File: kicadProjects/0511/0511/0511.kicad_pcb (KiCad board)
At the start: 2 copper layers, 102 parts, among them SW1 SW_Push, SW10 SW_Push, SW11 SW_Push, SW12 SW_Push, SW13 SW_Push, SW14 SW_Push, SW15 SW_Push, SW16 SW_Push, SW17 SW_Push, SW18 SW_Push, SW19 SW_Push, SW2 SW_Push, SW20 SW_Push, SW21 SW_Push, SW22 SW_Push, SW23 SW_Push, SW24 SW_Push, SW25 SW_Push, SW26 SW_Push, SW27 SW_Push, SW28 SW_Push, SW29 SW_Push, SW3 SW_Push, SW30 SW_Push, SW31 SW_Push, SW32 SW_Push, SW33 SW_Push, SW34 SW_Push, SW35 SW_Push, SW36 SW_Push, SW37 SW_Push, SW38 SW_Push, SW39 SW_Push, SW4 SW_Push, SW40 SW_Push, SW41 SW_Push, SW42 SW_Push, SW43 SW_Push, SW44 SW_Push, SW45 SW_Push, SW46 SW_Push, SW47 SW_Push, SW48 SW_Push, SW5 SW_Push, SW6 SW_Push, SW7 SW_Push, SW8 SW_Push, SW9 SW_Push, U1 MCP23017, U2 YAAJ_BlackPill, U3 MCP23017, U4 MCP23017

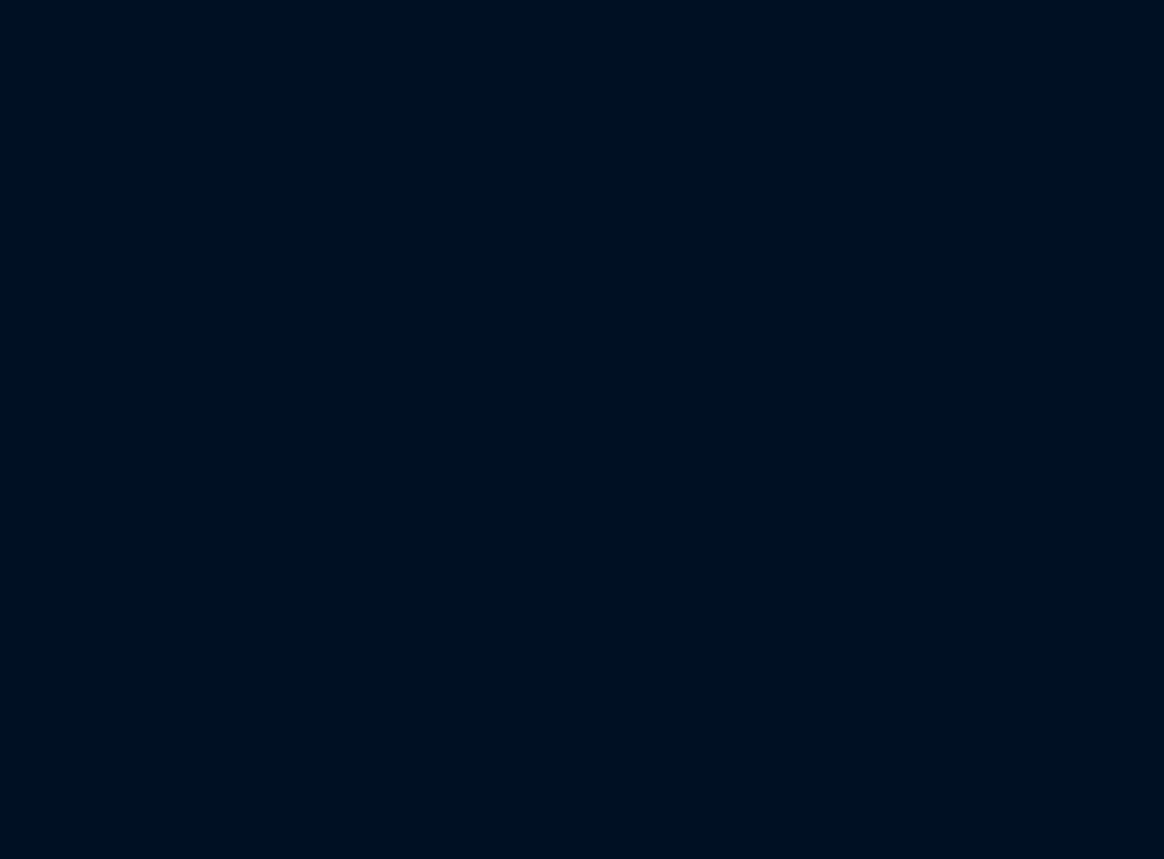
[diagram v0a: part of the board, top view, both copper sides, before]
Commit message: poursuite schema
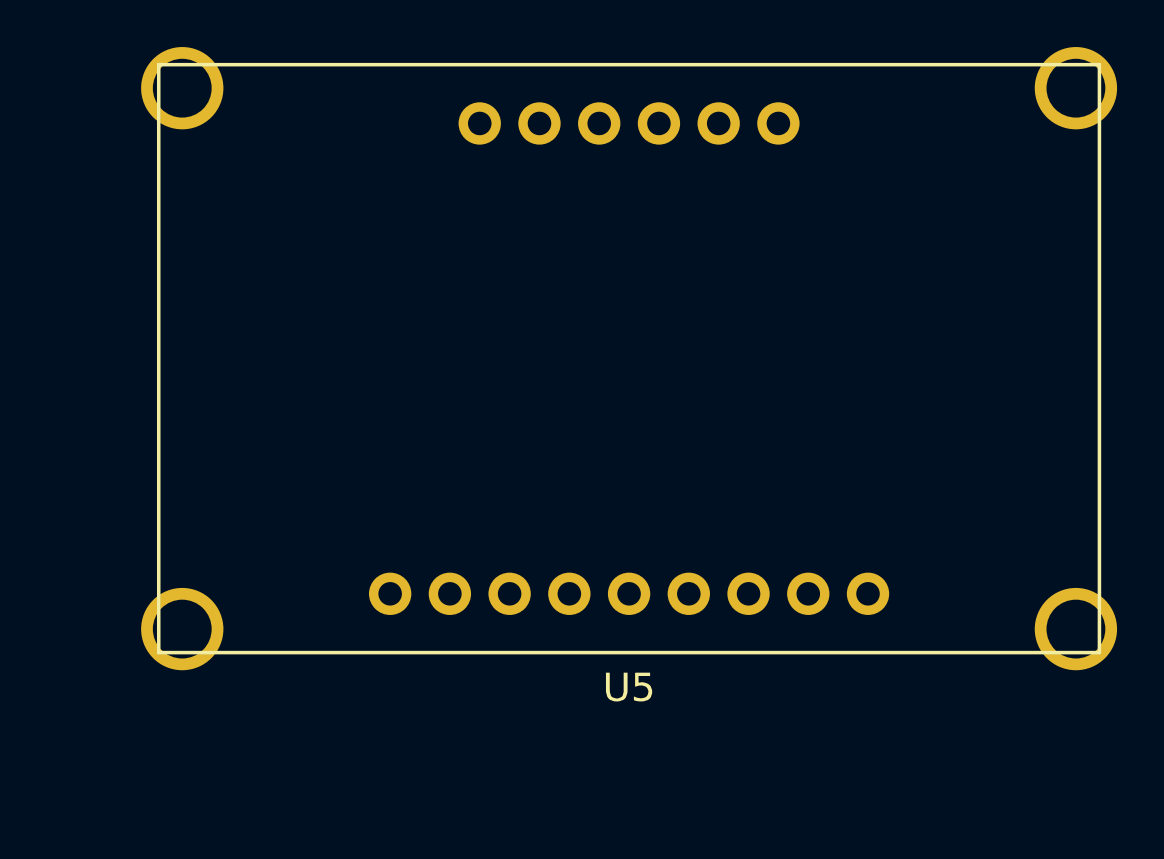
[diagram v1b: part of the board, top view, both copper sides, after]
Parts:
- added U5: UDA1334A_Breakout, Adafruit_UDA1334A:PinHeader_1x07_2.54mm, F.Cu at (244.0, 32.0)
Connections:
- U2 pad 27: unconnected-(U2-PA4-Pad27) -> Net-(U2-PA4)
- U2 pad 28: unconnected-(U2-PA5-Pad28) -> Net-(U2-PA5)
- U2 pad 30: unconnected-(U2-PA7-Pad30) -> Net-(U2-PA7)

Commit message: poursuite
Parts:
- moved U4 245.7 mm to (271.9, -77.1)
- moved R34 151.6 mm to (244.5, 90.5)
- moved SW29 115.0 mm to (240.5, 49.4)
- moved U5 108.0 mm to (302.1, 123.0)
- moved U2 94.7 mm to (238.0, 120.9)
- moved SW41 75.1 mm to (225.3, 49.6)
- moved SW35 75.1 mm to (210.2, 49.6)
- moved SW15 74.0 mm to (172.4, 35.0)
- moved SW21 74.0 mm to (187.5, 35.0)
- moved SW27 74.0 mm to (202.6, 35.0)
- moved SW3 74.0 mm to (142.2, 35.0)
- moved SW39 74.0 mm to (232.8, 35.0)
- moved SW9 74.0 mm to (157.3, 35.0)
- moved SW33 74.0 mm to (217.7, 35.0)
- moved SW12 70.3 mm to (143.2, 64.0)
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
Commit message: rectifications, modif empreinte capteur fsr, correctifs warnings
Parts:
- R1: value 4.7k -> R_Variable; footprint Resistor_THT:R_Axial_DIN0207_L6.3mm_D2.5mm_P7.62mm_Horizontal -> Connector_PinHeader_2.54mm:PinHeader_1x02_P2.54mm_Vertical
- R17, R33: value ~ -> R
- R19: value R -> ~
- R2: value 4.7k -> ~
- R3, R4: value R -> 4.7k
- R34: value R_Variable -> R; footprint Button_Switch_THT:Push_E-Switch_KS01Q01 -> Resistor_THT:R_Axial_DIN0207_L6.3mm_D2.5mm_P7.62mm_Horizontal
- U1: value MCP23017 -> UDA1334A_Breakout; footprint Package_DIP:DIP-28_W7.62mm -> Adafruit_UDA1334A:PinHeader_1x07_2.54mm
- U5: value UDA1334A_Breakout -> MCP23017; footprint Adafruit_UDA1334A:PinHeader_1x07_2.54mm -> Package_DIP:DIP-28_W7.62mm
- moved U4 221.4 mm to (163.5, 116.0)
- moved R34 164.1 mm to (88.1, 140.3)
- moved U5 128.1 mm to (174.3, 116.0)
- moved SW29 111.3 mm to (135.5, 86.2)
- moved U2 100.9 mm to (189.7, 32.4)
- moved R1 95.4 mm to (155.5, 155.5)
- moved SW15 70.4 mm to (105.3, 56.0)
- moved SW21 70.4 mm to (120.4, 56.0)
- moved SW27 70.4 mm to (135.5, 56.0)
- moved SW3 70.4 mm to (75.1, 56.0)
- moved SW39 70.4 mm to (165.6, 56.0)
- moved SW9 70.4 mm to (90.2, 56.0)
- moved SW33 70.4 mm to (150.6, 56.0)
- moved SW41 70.0 mm to (165.6, 86.2)
- moved SW35 70.0 mm to (150.6, 86.2)
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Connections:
- R1 pad 1: Net-(R1-Pad1) -> Net-(U1-3V)
- R1 pad 2: Net-(U1-A0) -> Net-(U2-PA1)
- R10 pad 2: Net-(U1-A0) -> Net-(U3-A0)
- R11 pad 2: Net-(U1-A0) -> Net-(U3-A0)
- R12 pad 2: Net-(U1-A0) -> Net-(U3-A0)
- R13 pad 2: Net-(U1-A0) -> Net-(U3-A0)
- R14 pad 2: Net-(U1-A0) -> Net-(U3-A0)
- R15 pad 2: Net-(U1-A0) -> Net-(U3-A0)
- R16 pad 2: Net-(U1-A0) -> Net-(U3-A0)
- R17 pad 2: Net-(R17-Pad2) -> Net-(U3-A0)
- R18 pad 2: Net-(R17-Pad2) -> Net-(U3-A0)
- R19 pad 2: Net-(R17-Pad2) -> Net-(R19-Pad2)
- R2 pad 1: Net-(R2-Pad1) -> Net-(U2-PA1)
- R2 pad 2: Net-(U1-A0) -> Net-(U3-A0)
- R20 pad 2: Net-(R17-Pad2) -> Net-(R19-Pad2)
- R21 pad 2: Net-(R17-Pad2) -> Net-(R19-Pad2)
- R22 pad 2: Net-(R17-Pad2) -> Net-(R19-Pad2)
- R23 pad 2: Net-(R17-Pad2) -> Net-(R19-Pad2)
- R24 pad 2: Net-(R17-Pad2) -> Net-(R19-Pad2)
- R25 pad 2: Net-(R17-Pad2) -> Net-(R19-Pad2)
- R26 pad 2: Net-(U1-A0) -> Net-(R19-Pad2)
- R27 pad 2: Net-(U1-A0) -> Net-(R19-Pad2)
- R28 pad 2: Net-(U1-A0) -> Net-(U3-A0)
- R29 pad 2: Net-(U1-A0) -> Net-(U3-A0)
- R3 pad 2: Net-(U1-A0) -> Net-(U3-A0)
- R30 pad 2: Net-(U1-A0) -> Net-(U3-A0)
- R31 pad 2: Net-(U1-A0) -> Net-(U3-A0)
- R32 pad 2: Net-(U1-A0) -> Net-(U3-A0)
- R33 pad 2: Net-(U1-A0) -> Net-(U3-A0)
- R34 pad 1: Net-(U1-SCL) -> Net-(R34-Pad1)
- R34 pad 2: Net-(U2-PA1) -> Net-(U3-A0)
- R35 pad 1: Net-(U2-PA1) -> Net-(R35-Pad1)
- R35 pad 2: Net-(U1-A0) -> Net-(U3-A0)
- R36 pad 2: Net-(U1-A0) -> Net-(U3-A0)
- R37 pad 2: Net-(U1-A0) -> Net-(U3-A0)
- R38 pad 2: Net-(U1-A0) -> Net-(U3-A0)
- R39 pad 2: Net-(U1-A0) -> Net-(U3-A0)
- R4 pad 2: Net-(U1-A0) -> Net-(U3-A0)
- R40 pad 2: Net-(U1-A0) -> Net-(U3-A0)
- R41 pad 2: Net-(U1-A0) -> Net-(U3-A0)
- R42 pad 2: Net-(U1-A0) -> Net-(U3-A0)
- R43 pad 2: Net-(U1-A0) -> Net-(U3-A0)
- R44 pad 2: Net-(U1-A0) -> Net-(U3-A0)
- R45 pad 2: Net-(U1-A0) -> Net-(U3-A0)
- R46 pad 2: Net-(U1-A0) -> Net-(U3-A0)
- R47 pad 2: Net-(U1-A0) -> Net-(U3-A0)
- R48 pad 2: Net-(U1-A0) -> Net-(U3-A0)
- R49 pad 2: Net-(U1-A0) -> Net-(U3-A0)
- R5 pad 2: Net-(U1-A0) -> Net-(U3-A0)
- R50 pad 2: Net-(U1-A0) -> Net-(U3-A0)
- R6 pad 2: Net-(U1-A0) -> Net-(U3-A0)
- R7 pad 2: Net-(U1-A0) -> Net-(U3-A0)
- R8 pad 2: Net-(U1-A0) -> Net-(U3-A0)
- R9 pad 2: Net-(U1-A0) -> Net-(U3-A0)
- SW1 pad 1: Net-(R1-Pad1) -> Net-(R3-Pad1)
- SW1 pad 2: Net-(U1-GPA7) -> Net-(U3-GPA7)
- SW10 pad 1: Net-(R10-Pad1) -> Net-(R12-Pad1)
- SW10 pad 2: Net-(U1-GPB6) -> Net-(U3-GPB6)
- SW11 pad 1: Net-(R11-Pad1) -> Net-(R13-Pad1)
- SW11 pad 2: Net-(U1-GPB5) -> Net-(U3-GPB5)
- SW12 pad 1: Net-(R12-Pad1) -> Net-(R14-Pad1)
- SW12 pad 2: Net-(U1-GPB4) -> Net-(U3-GPB4)
- SW13 pad 1: Net-(R13-Pad1) -> Net-(R15-Pad1)
- SW13 pad 2: Net-(U1-GPB3) -> Net-(U3-GPB3)
- SW14 pad 1: Net-(R14-Pad1) -> Net-(R16-Pad1)
- SW14 pad 2: Net-(U1-GPB2) -> Net-(U3-GPB2)
- SW15 pad 1: Net-(R15-Pad1) -> Net-(R17-Pad1)
- SW15 pad 2: Net-(U1-GPB1) -> Net-(U3-GPB1)
- SW16 pad 1: Net-(R16-Pad1) -> Net-(R18-Pad1)
- SW16 pad 2: Net-(U1-GPB0) -> Net-(U3-GPB0)
- SW17 pad 1: Net-(R17-Pad1) -> Net-(R19-Pad1)
- SW17 pad 2: Net-(U3-GPA7) -> Net-(U4-GPA7)
- SW18 pad 1: Net-(R18-Pad1) -> Net-(R20-Pad1)
- SW18 pad 2: Net-(U3-GPA6) -> Net-(U4-GPA6)
- SW19 pad 1: Net-(R19-Pad1) -> Net-(R21-Pad1)
- SW19 pad 2: Net-(U3-GPA5) -> Net-(U4-GPA5)
- SW2 pad 1: Net-(R2-Pad1) -> Net-(R4-Pad1)
- SW2 pad 2: Net-(U1-GPA6) -> Net-(U3-GPA6)
- SW20 pad 1: Net-(R20-Pad1) -> Net-(R22-Pad1)
- SW20 pad 2: Net-(U3-GPA4) -> Net-(U4-GPA4)
- SW21 pad 1: Net-(R21-Pad1) -> Net-(R23-Pad1)
- SW21 pad 2: Net-(U3-GPA3) -> Net-(U4-GPA3)
- SW22 pad 1: Net-(R22-Pad1) -> Net-(R24-Pad1)
- SW22 pad 2: Net-(U3-GPA2) -> Net-(U4-GPA2)
- SW23 pad 1: Net-(R23-Pad1) -> Net-(R25-Pad1)
- SW23 pad 2: Net-(U3-GPA1) -> Net-(U4-GPA1)
- SW24 pad 1: Net-(R24-Pad1) -> Net-(R26-Pad1)
- SW24 pad 2: Net-(U3-GPA0) -> Net-(U4-GPA0)
- SW25 pad 1: Net-(R25-Pad1) -> Net-(R27-Pad1)
- SW25 pad 2: Net-(U3-GPB7) -> Net-(U4-GPB7)
- SW26 pad 1: Net-(R26-Pad1) -> Net-(R28-Pad1)
- SW26 pad 2: Net-(U3-GPB6) -> Net-(U4-GPB6)
- SW27 pad 1: Net-(R27-Pad1) -> Net-(R29-Pad1)
- SW27 pad 2: Net-(U3-GPB5) -> Net-(U4-GPB5)
- SW28 pad 1: Net-(R28-Pad1) -> Net-(R30-Pad1)
- SW28 pad 2: Net-(U3-GPB4) -> Net-(U4-GPB4)
- SW29 pad 1: Net-(R29-Pad1) -> Net-(R31-Pad1)
- SW29 pad 2: Net-(U3-GPB3) -> Net-(U4-GPB3)
- SW3 pad 1: Net-(R3-Pad1) -> Net-(R5-Pad1)
- SW3 pad 2: Net-(U1-GPA5) -> Net-(U3-GPA5)
- SW30 pad 1: Net-(R30-Pad1) -> Net-(R32-Pad1)
- SW30 pad 2: Net-(U3-GPB2) -> Net-(U4-GPB2)
- SW31 pad 1: Net-(R31-Pad1) -> Net-(R33-Pad1)
- SW31 pad 2: Net-(U3-GPB1) -> Net-(U4-GPB1)
- SW32 pad 1: Net-(R32-Pad1) -> Net-(R34-Pad1)
- SW32 pad 2: Net-(U3-GPB0) -> Net-(U4-GPB0)
- SW33 pad 1: Net-(R33-Pad1) -> Net-(R35-Pad1)
- SW33 pad 2: Net-(U4-GPA7) -> Net-(U5-GPA7)
- SW34 pad 2: Net-(U4-GPA6) -> Net-(U5-GPA6)
- SW35 pad 2: Net-(U4-GPA5) -> Net-(U5-GPA5)
- SW36 pad 2: Net-(U4-GPA4) -> Net-(U5-GPA4)
- SW37 pad 2: Net-(U4-GPA3) -> Net-(U5-GPA3)
- SW38 pad 2: Net-(U4-GPA2) -> Net-(U5-GPA2)
- SW39 pad 2: Net-(U4-GPA1) -> Net-(U5-GPA1)
- SW4 pad 1: Net-(R4-Pad1) -> Net-(R6-Pad1)
- SW4 pad 2: Net-(U1-GPA4) -> Net-(U3-GPA4)
- SW40 pad 2: Net-(U4-GPA0) -> Net-(U5-GPA0)
- SW41 pad 2: Net-(U4-GPB7) -> Net-(U5-GPB7)
- SW42 pad 2: Net-(U4-GPB6) -> Net-(U5-GPB6)
- SW43 pad 2: Net-(U4-GPB5) -> Net-(U5-GPB5)
- SW44 pad 2: Net-(U4-GPB4) -> Net-(U5-GPB4)
- SW45 pad 2: Net-(U4-GPB3) -> Net-(U5-GPB3)
- SW46 pad 2: Net-(U4-GPB2) -> Net-(U5-GPB2)
- SW47 pad 2: Net-(U4-GPB1) -> Net-(U5-GPB1)
- SW48 pad 2: Net-(U4-GPB0) -> Net-(U5-GPB0)
- SW5 pad 1: Net-(R5-Pad1) -> Net-(R7-Pad1)
- SW5 pad 2: Net-(U1-GPA3) -> Net-(U3-GPA3)
- SW6 pad 1: Net-(R6-Pad1) -> Net-(R8-Pad1)
- SW6 pad 2: Net-(U1-GPA2) -> Net-(U3-GPA2)
- SW7 pad 1: Net-(R7-Pad1) -> Net-(R9-Pad1)
- SW7 pad 2: Net-(U1-GPA1) -> Net-(U3-GPA1)
- SW8 pad 1: Net-(R8-Pad1) -> Net-(R10-Pad1)
- SW8 pad 2: Net-(U1-GPA0) -> Net-(U3-GPA0)
- SW9 pad 1: Net-(R9-Pad1) -> Net-(R11-Pad1)
- SW9 pad 2: Net-(U1-GPB7) -> Net-(U3-GPB7)
- U1 pad 1: Net-(U1-GPB0) -> unconnected-(U1-VIN-Pad1)
- U1 pad 10: unconnected-(U1-VSS-Pad10) -> (no net)
- U1 pad 11: unconnected-(U1-NC-Pad11) -> (no net)
- U1 pad 12: Net-(U1-SCL) -> (no net)
- U1 pad 13: Net-(U1-SCL) -> (no net)
- U1 pad 14: unconnected-(U1-NC-Pad14) -> (no net)
- U1 pad 15: Net-(U1-A0) -> (no net)
- U1 pad 2: Net-(U1-GPB1) -> Net-(U1-3V)
- U1 pad 3: Net-(U1-GPB2) -> unconnected-(U1-GND-Pad3)
- U1 pad 4: Net-(U1-GPB3) -> Net-(U1-WSEL)
- U1 pad 5: Net-(U1-GPB4) -> Net-(U1-BCLK)
- U1 pad 6: Net-(U1-GPB5) -> Net-(U1-DIN)
- U1 pad 7: Net-(U1-GPB6) -> (no net)
- U1 pad 8: Net-(U1-GPB7) -> (no net)
- U1 pad 9: unconnected-(U1-VDD-Pad9) -> (no net)
- U2 pad 16: Net-(U1-SCL) -> Net-(U1-3V)
- U2 pad 17: Net-(U1-A0) -> Net-(U3-A0)
- U2 pad 18: Net-(U1-A0) -> Net-(U3-A0)
- U2 pad 19: Net-(U1-SCL) -> Net-(U1-3V)
- U2 pad 20: Net-(U1-SCL) -> Net-(U1-3V)
- U2 pad 27: Net-(U2-PA4) -> Net-(U1-WSEL)
- U2 pad 28: Net-(U2-PA5) -> Net-(U1-BCLK)
- U2 pad 30: Net-(U2-PA7) -> Net-(U1-DIN)
- U3 pad 12: Net-(U1-SCL) -> Net-(U1-3V)
- U3 pad 13: Net-(U1-SCL) -> Net-(U1-3V)
- U3 pad 15: Net-(U1-A0) -> Net-(U3-A0)
- U3 pad 16: Net-(U1-SCL) -> Net-(U3-A0)
- U3 pad 17: Net-(U1-SCL) -> Net-(U3-A0)
- U4 pad 12: Net-(U1-SCL) -> Net-(U1-3V)
- U4 pad 13: Net-(U1-SCL) -> Net-(U1-3V)
- U4 pad 15: Net-(U1-SCL) -> Net-(U3-A0)
- U4 pad 16: Net-(U1-SCL) -> Net-(U1-3V)
- U4 pad 17: Net-(U1-SCL) -> Net-(U1-3V)
- U4 pad 18: Net-(U1-SCL) -> unconnected-(U4-~{RESET}-Pad18)
- U4 pad 19: Net-(U1-SCL) -> unconnected-(U4-INTB-Pad19)
- U4 pad 20: Net-(U1-SCL) -> unconnected-(U4-INTA-Pad20)
- U5 pad 1: unconnected-(U5-VIN-Pad1) -> Net-(U5-GPB0)
- U5 pad 10: (no net) -> unconnected-(U5-VSS-Pad10)
- U5 pad 11: (no net) -> unconnected-(U5-NC-Pad11)
- U5 pad 12: (no net) -> Net-(U1-3V)
- U5 pad 13: (no net) -> Net-(U1-3V)
- U5 pad 14: (no net) -> unconnected-(U5-NC-Pad14)
- U5 pad 15: (no net) -> Net-(U1-3V)
- U5 pad 2: Net-(U1-SCL) -> Net-(U5-GPB1)
- U5 pad 3: unconnected-(U5-GND-Pad3) -> Net-(U5-GPB2)
- U5 pad 4: Net-(U2-PA4) -> Net-(U5-GPB3)
- U5 pad 5: Net-(U2-PA5) -> Net-(U5-GPB4)
- U5 pad 6: Net-(U2-PA7) -> Net-(U5-GPB5)
- U5 pad 7: (no net) -> Net-(U5-GPB6)
- U5 pad 8: (no net) -> Net-(U5-GPB7)
- U5 pad 9: (no net) -> unconnected-(U5-VDD-Pad9)

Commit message: ajout empreintes
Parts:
- removed R41, R42, R43, R44, R45, R46, R47, R48, R49, R50: R, Resistor_THT:R_Axial_DIN0207_L6.3mm_D2.5mm_P7.62mm_Horizontal
- removed SW33, SW34, SW35, SW36, SW37, SW38, SW39, SW40, SW41, SW42, SW43, SW44, SW45, SW46, SW47, SW48: SW_Push, Button_Switch_Keyboard:SW_Cherry_MX_1.00u_PCB
- removed U5: MCP23017, Package_DIP:DIP-28_W7.62mm
- added C1: C, Capacitor_THT:C_Disc_D3.0mm_W1.6mm_P2.50mm, F.Cu at (287.0, 157.0)
- added C10: C, Capacitor_THT:C_Disc_D3.0mm_W1.6mm_P2.50mm, F.Cu at (271.1, 142.4)
- added C11: C, Capacitor_THT:C_Disc_D3.0mm_W1.6mm_P2.50mm, F.Cu at (255.2, 133.1)
- added C12: C, Capacitor_THT:C_Disc_D3.0mm_W1.6mm_P2.50mm, F.Cu at (239.3, 133.1)
- added C13: C, Capacitor_THT:C_Disc_D3.0mm_W1.6mm_P2.50mm, F.Cu at (223.4, 95.5)
- added C14: C, Capacitor_THT:C_Disc_D3.0mm_W1.6mm_P2.50mm, F.Cu at (271.1, 133.1)
- added C15: C, Capacitor_THT:C_Disc_D3.0mm_W1.6mm_P2.50mm, F.Cu at (223.4, 133.1)
- added C16: C, Capacitor_THT:C_Disc_D3.0mm_W1.6mm_P2.50mm, F.Cu at (223.4, 161.2)
- added C17: C, Capacitor_THT:C_Disc_D3.0mm_W1.6mm_P2.50mm, F.Cu at (271.1, 151.8)
- added C18: C, Capacitor_THT:C_Disc_D3.0mm_W1.6mm_P2.50mm, F.Cu at (223.4, 114.2)
- added C19: C, Capacitor_THT:C_Disc_D3.0mm_W1.6mm_P2.50mm, F.Cu at (255.2, 123.7)
- added C2: C, Capacitor_THT:C_Disc_D3.0mm_W1.6mm_P2.50mm, F.Cu at (255.2, 161.2)
- added C20: C, Capacitor_THT:C_Disc_D3.0mm_W1.6mm_P2.50mm, F.Cu at (271.1, 114.2)
- added C21: C, Capacitor_THT:C_Disc_D3.0mm_W1.6mm_P2.50mm, F.Cu at (271.1, 104.8)
- added C22: C, Capacitor_THT:C_Disc_D3.0mm_W1.6mm_P2.50mm, F.Cu at (271.1, 161.2)
- added C23: C, Capacitor_THT:C_Disc_D3.0mm_W1.6mm_P2.50mm, F.Cu at (223.4, 142.4)
- added C24: C, Capacitor_THT:C_Disc_D3.0mm_W1.6mm_P2.50mm, F.Cu at (239.3, 123.7)
- added C25: C, Capacitor_THT:C_Disc_D3.0mm_W1.6mm_P2.50mm, F.Cu at (239.3, 151.8)
- added C26: C, Capacitor_THT:C_Disc_D3.0mm_W1.6mm_P2.50mm, F.Cu at (239.3, 142.4)
- added C27: C, Capacitor_THT:C_Disc_D3.0mm_W1.6mm_P2.50mm, F.Cu at (255.2, 95.5)
- added C28: C, Capacitor_THT:C_Disc_D3.0mm_W1.6mm_P2.50mm, F.Cu at (223.4, 104.8)
- added C29: C, Capacitor_THT:C_Disc_D3.0mm_W1.6mm_P2.50mm, F.Cu at (239.3, 104.8)
- added C3: C, Capacitor_THT:C_Disc_D3.0mm_W1.6mm_P2.50mm, F.Cu at (223.4, 123.7)
- added C30: C, Capacitor_THT:C_Disc_D3.0mm_W1.6mm_P2.50mm, F.Cu at (223.4, 151.8)
- added C31: C, Capacitor_THT:C_Disc_D3.0mm_W1.6mm_P2.50mm, F.Cu at (239.3, 95.5)
- added C32: C, Capacitor_THT:C_Disc_D3.0mm_W1.6mm_P2.50mm, F.Cu at (271.1, 123.7)
- added C33: C, Capacitor_THT:C_Disc_D3.0mm_W1.6mm_P2.50mm, F.Cu at (239.3, 161.2)
- added C4: C, Capacitor_THT:C_Disc_D3.0mm_W1.6mm_P2.50mm, F.Cu at (239.3, 114.2)
- added C5: C, Capacitor_THT:C_Disc_D3.0mm_W1.6mm_P2.50mm, F.Cu at (255.2, 104.8)
- added C6: C, Capacitor_THT:C_Disc_D3.0mm_W1.6mm_P2.50mm, F.Cu at (271.1, 95.5)
- added C7: C, Capacitor_THT:C_Disc_D3.0mm_W1.6mm_P2.50mm, F.Cu at (255.2, 114.2)
- added C8: C, Capacitor_THT:C_Disc_D3.0mm_W1.6mm_P2.50mm, F.Cu at (255.2, 142.4)
- added C9: C, Capacitor_THT:C_Disc_D3.0mm_W1.6mm_P2.50mm, F.Cu at (255.2, 151.8)
- added D1: LED, Diode_THT:D_DO-41_SOD81_P10.16mm_Horizontal, F.Cu at (255.5, 157.6)
- added D10: LED, Diode_THT:D_DO-41_SOD81_P10.16mm_Horizontal, F.Cu at (255.5, 129.3)
- added D11: LED, Diode_THT:D_DO-41_SOD81_P10.16mm_Horizontal, F.Cu at (239.6, 129.3)
- added D12: LED, Diode_THT:D_DO-41_SOD81_P10.16mm_Horizontal, F.Cu at (223.7, 91.8)
- added D13: LED, Diode_THT:D_DO-41_SOD81_P10.16mm_Horizontal, F.Cu at (271.4, 129.3)
- added D14: LED, Diode_THT:D_DO-41_SOD81_P10.16mm_Horizontal, F.Cu at (223.7, 129.3)
- added D15: LED, Diode_THT:D_DO-41_SOD81_P10.16mm_Horizontal, F.Cu at (223.7, 157.6)
- added D16: LED, Diode_THT:D_DO-41_SOD81_P10.16mm_Horizontal, F.Cu at (271.4, 148.2)
- added D17: LED, Diode_THT:D_DO-41_SOD81_P10.16mm_Horizontal, F.Cu at (223.7, 110.5)
- added D18: LED, Diode_THT:D_DO-41_SOD81_P10.16mm_Horizontal, F.Cu at (255.5, 120.0)
- added D19: LED, Diode_THT:D_DO-41_SOD81_P10.16mm_Horizontal, F.Cu at (271.4, 110.5)
- added D2: LED, Diode_THT:D_DO-41_SOD81_P10.16mm_Horizontal, F.Cu at (223.7, 120.0)
- added D20: LED, Diode_THT:D_DO-41_SOD81_P10.16mm_Horizontal, F.Cu at (271.4, 101.2)
- added D21: LED, Diode_THT:D_DO-41_SOD81_P10.16mm_Horizontal, F.Cu at (271.4, 157.6)
- added D22: LED, Diode_THT:D_DO-41_SOD81_P10.16mm_Horizontal, F.Cu at (223.7, 138.8)
- added D23: LED, Diode_THT:D_DO-41_SOD81_P10.16mm_Horizontal, F.Cu at (239.6, 120.0)
- added D24: LED, Diode_THT:D_DO-41_SOD81_P10.16mm_Horizontal, F.Cu at (239.6, 148.2)
- added D25: LED, Diode_THT:D_DO-41_SOD81_P10.16mm_Horizontal, F.Cu at (239.6, 138.8)
- added D26: LED, Diode_THT:D_DO-41_SOD81_P10.16mm_Horizontal, F.Cu at (255.5, 91.8)
- added D27: LED, Diode_THT:D_DO-41_SOD81_P10.16mm_Horizontal, F.Cu at (223.7, 101.2)
- added D28: LED, Diode_THT:D_DO-41_SOD81_P10.16mm_Horizontal, F.Cu at (239.6, 101.2)
- added D29: LED, Diode_THT:D_DO-41_SOD81_P10.16mm_Horizontal, F.Cu at (223.7, 148.2)
- added D3: LED, Diode_THT:D_DO-41_SOD81_P10.16mm_Horizontal, F.Cu at (239.6, 110.5)
- added D30: LED, Diode_THT:D_DO-41_SOD81_P10.16mm_Horizontal, F.Cu at (239.6, 91.8)
- added D31: LED, Diode_THT:D_DO-41_SOD81_P10.16mm_Horizontal, F.Cu at (271.4, 120.0)
- added D32: LED, Diode_THT:D_DO-41_SOD81_P10.16mm_Horizontal, F.Cu at (239.6, 157.6)
- added D4: LED, Diode_THT:D_DO-41_SOD81_P10.16mm_Horizontal, F.Cu at (255.5, 101.2)
- added D5: LED, Diode_THT:D_DO-41_SOD81_P10.16mm_Horizontal, F.Cu at (271.4, 91.8)
- added D6: LED, Diode_THT:D_DO-41_SOD81_P10.16mm_Horizontal, F.Cu at (255.5, 110.5)
- added D7: LED, Diode_THT:D_DO-41_SOD81_P10.16mm_Horizontal, F.Cu at (255.5, 138.8)
- added D8: LED, Diode_THT:D_DO-41_SOD81_P10.16mm_Horizontal, F.Cu at (255.5, 148.2)
- added D9: LED, Diode_THT:D_DO-41_SOD81_P10.16mm_Horizontal, F.Cu at (271.4, 138.8)
- R1: footprint Connector_PinHeader_2.54mm:PinHeader_1x02_P2.54mm_Vertical -> Button_Switch_THT:Push_E-Switch_KS01Q01
- R19, R35: value ~ -> R
- R3, R4: value 4.7k -> R
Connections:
- R10 pad 1: Net-(R10-Pad1) -> /Button_RCD1/To_MCP_PIN
- R10 pad 2: Net-(U3-A0) -> GND
- R11 pad 1: Net-(R11-Pad1) -> /Button_RCD2/To_MCP_PIN
- R11 pad 2: Net-(U3-A0) -> GND
- R12 pad 1: Net-(R12-Pad1) -> /Button_RCD3/To_MCP_PIN
- R12 pad 2: Net-(U3-A0) -> GND
- R13 pad 1: Net-(R13-Pad1) -> /Button_RCD4/To_MCP_PIN
- R13 pad 2: Net-(U3-A0) -> GND
- R14 pad 1: Net-(R14-Pad1) -> /Button_RCD5/To_MCP_PIN
- R14 pad 2: Net-(U3-A0) -> GND
- R15 pad 1: Net-(R15-Pad1) -> /Button_RCD6/To_MCP_PIN
- R15 pad 2: Net-(U3-A0) -> GND
- R16 pad 1: Net-(R16-Pad1) -> /Button_RCD7/To_MCP_PIN
- R16 pad 2: Net-(U3-A0) -> GND
- R17 pad 1: Net-(R17-Pad1) -> /Button_RCD8/To_MCP_PIN
- R17 pad 2: Net-(U3-A0) -> GND
- R18 pad 1: Net-(R18-Pad1) -> /Button_RCD9/To_MCP_PIN
- R18 pad 2: Net-(U3-A0) -> GND
- R19 pad 1: Net-(R19-Pad1) -> /Button_RCD10/To_MCP_PIN
- R19 pad 2: Net-(R19-Pad2) -> GND
- R2 pad 2: Net-(U3-A0) -> Net-(R2-Pad2)
- R20 pad 1: Net-(R20-Pad1) -> /Button_RCD11/To_MCP_PIN
- R20 pad 2: Net-(R19-Pad2) -> GND
- R21 pad 1: Net-(R21-Pad1) -> /Button_RCD12/To_MCP_PIN
- R21 pad 2: Net-(R19-Pad2) -> GND
- R22 pad 1: Net-(R22-Pad1) -> /Button_RCD13/To_MCP_PIN
- R22 pad 2: Net-(R19-Pad2) -> GND
- R23 pad 1: Net-(R23-Pad1) -> /Button_RCD14/To_MCP_PIN
- R23 pad 2: Net-(R19-Pad2) -> GND
- R24 pad 1: Net-(R24-Pad1) -> /Button_RCD15/To_MCP_PIN
- R24 pad 2: Net-(R19-Pad2) -> GND
- R25 pad 1: Net-(R25-Pad1) -> /Button_RCD16/To_MCP_PIN
- R25 pad 2: Net-(R19-Pad2) -> GND
- R26 pad 1: Net-(R26-Pad1) -> /Button_RCD17/To_MCP_PIN
- R26 pad 2: Net-(R19-Pad2) -> GND
- R27 pad 1: Net-(R27-Pad1) -> /Button_RCD18/To_MCP_PIN
- R27 pad 2: Net-(R19-Pad2) -> GND
- R28 pad 1: Net-(R28-Pad1) -> /Button_RCD19/To_MCP_PIN
- R28 pad 2: Net-(U3-A0) -> GND
- R29 pad 1: Net-(R29-Pad1) -> /Button_RCD20/To_MCP_PIN
- R29 pad 2: Net-(U3-A0) -> GND
- R3 pad 1: Net-(R3-Pad1) -> +3.3V
- R3 pad 2: Net-(U3-A0) -> Net-(U2-PB8)
- R30 pad 1: Net-(R30-Pad1) -> /Button_RCD21/To_MCP_PIN
- R30 pad 2: Net-(U3-A0) -> GND
- R31 pad 1: Net-(R31-Pad1) -> /Button_RCD22/To_MCP_PIN
- R31 pad 2: Net-(U3-A0) -> GND
- R32 pad 1: Net-(R32-Pad1) -> /Button_RCD23/To_MCP_PIN
- R32 pad 2: Net-(U3-A0) -> GND
- R33 pad 1: Net-(R33-Pad1) -> /Button_RCD24/To_MCP_PIN
- R33 pad 2: Net-(U3-A0) -> GND
- R34 pad 1: Net-(R34-Pad1) -> /Button_RCD25/To_MCP_PIN
- R34 pad 2: Net-(U3-A0) -> GND
- R35 pad 1: Net-(R35-Pad1) -> /Button_RCD26/To_MCP_PIN
- R35 pad 2: Net-(U3-A0) -> GND
- R36 pad 1: Net-(R36-Pad1) -> /Button_RCD27/To_MCP_PIN
- R36 pad 2: Net-(U3-A0) -> GND
- R37 pad 1: Net-(R37-Pad1) -> /Button_RCD28/To_MCP_PIN
- R37 pad 2: Net-(U3-A0) -> GND
- R38 pad 1: Net-(R38-Pad1) -> /Button_RCD29/To_MCP_PIN
- R38 pad 2: Net-(U3-A0) -> GND
- R39 pad 1: Net-(R39-Pad1) -> /Button_RCD30/To_MCP_PIN
- R39 pad 2: Net-(U3-A0) -> GND
- R4 pad 1: Net-(R4-Pad1) -> +3.3V
- R4 pad 2: Net-(U3-A0) -> Net-(U2-PB9)
- R40 pad 1: Net-(R40-Pad1) -> /Button_RCD31/To_MCP_PIN
- R40 pad 2: Net-(U3-A0) -> GND
- R5 pad 1: Net-(R5-Pad1) -> +3.3V
- R5 pad 2: Net-(U3-A0) -> Net-(U3-~{RESET})
- R6 pad 1: Net-(R6-Pad1) -> +3.3V
- R6 pad 2: Net-(U3-A0) -> Net-(U2-PB8)
- R7 pad 1: Net-(R7-Pad1) -> +3.3V
- R7 pad 2: Net-(U3-A0) -> Net-(U4-~{RESET})
- R8 pad 1: Net-(R8-Pad1) -> +3.3V
- R8 pad 2: Net-(U3-A0) -> Net-(U2-PB9)
- R9 pad 1: Net-(R9-Pad1) -> /Button_RCD/To_MCP_PIN
- R9 pad 2: Net-(U3-A0) -> GND
- SW1 pad 1: Net-(R3-Pad1) -> +3.3V
- SW1 pad 2: Net-(U3-GPA7) -> /Button_RCD/To_MCP_PIN
- SW10 pad 1: Net-(R12-Pad1) -> +3.3V
- SW10 pad 2: Net-(U3-GPB6) -> /Button_RCD9/To_MCP_PIN
- SW11 pad 1: Net-(R13-Pad1) -> +3.3V
- SW11 pad 2: Net-(U3-GPB5) -> /Button_RCD10/To_MCP_PIN
- SW12 pad 1: Net-(R14-Pad1) -> +3.3V
- SW12 pad 2: Net-(U3-GPB4) -> /Button_RCD11/To_MCP_PIN
- SW13 pad 1: Net-(R15-Pad1) -> +3.3V
- SW13 pad 2: Net-(U3-GPB3) -> /Button_RCD12/To_MCP_PIN
- SW14 pad 1: Net-(R16-Pad1) -> +3.3V
- SW14 pad 2: Net-(U3-GPB2) -> /Button_RCD13/To_MCP_PIN
- SW15 pad 1: Net-(R17-Pad1) -> +3.3V
- SW15 pad 2: Net-(U3-GPB1) -> /Button_RCD14/To_MCP_PIN
- SW16 pad 1: Net-(R18-Pad1) -> +3.3V
- SW16 pad 2: Net-(U3-GPB0) -> /Button_RCD15/To_MCP_PIN
- SW17 pad 1: Net-(R19-Pad1) -> +3.3V
- SW17 pad 2: Net-(U4-GPA7) -> /Button_RCD16/To_MCP_PIN
- SW18 pad 1: Net-(R20-Pad1) -> +3.3V
- SW18 pad 2: Net-(U4-GPA6) -> /Button_RCD17/To_MCP_PIN
- SW19 pad 1: Net-(R21-Pad1) -> +3.3V
- SW19 pad 2: Net-(U4-GPA5) -> /Button_RCD18/To_MCP_PIN
- SW2 pad 1: Net-(R4-Pad1) -> +3.3V
- SW2 pad 2: Net-(U3-GPA6) -> /Button_RCD1/To_MCP_PIN
- SW20 pad 1: Net-(R22-Pad1) -> +3.3V
- SW20 pad 2: Net-(U4-GPA4) -> /Button_RCD19/To_MCP_PIN
- SW21 pad 1: Net-(R23-Pad1) -> +3.3V
- SW21 pad 2: Net-(U4-GPA3) -> /Button_RCD20/To_MCP_PIN
- SW22 pad 1: Net-(R24-Pad1) -> +3.3V
- SW22 pad 2: Net-(U4-GPA2) -> /Button_RCD21/To_MCP_PIN
- SW23 pad 1: Net-(R25-Pad1) -> +3.3V
- SW23 pad 2: Net-(U4-GPA1) -> /Button_RCD22/To_MCP_PIN
- SW24 pad 1: Net-(R26-Pad1) -> +3.3V
- SW24 pad 2: Net-(U4-GPA0) -> /Button_RCD23/To_MCP_PIN
- SW25 pad 1: Net-(R27-Pad1) -> +3.3V
- SW25 pad 2: Net-(U4-GPB7) -> /Button_RCD24/To_MCP_PIN
- SW26 pad 1: Net-(R28-Pad1) -> +3.3V
- SW26 pad 2: Net-(U4-GPB6) -> /Button_RCD25/To_MCP_PIN
- SW27 pad 1: Net-(R29-Pad1) -> +3.3V
- SW27 pad 2: Net-(U4-GPB5) -> /Button_RCD26/To_MCP_PIN
- SW28 pad 1: Net-(R30-Pad1) -> +3.3V
- SW28 pad 2: Net-(U4-GPB4) -> /Button_RCD27/To_MCP_PIN
- SW29 pad 1: Net-(R31-Pad1) -> +3.3V
- SW29 pad 2: Net-(U4-GPB3) -> /Button_RCD28/To_MCP_PIN
- SW3 pad 1: Net-(R5-Pad1) -> +3.3V
- SW3 pad 2: Net-(U3-GPA5) -> /Button_RCD2/To_MCP_PIN
- SW30 pad 1: Net-(R32-Pad1) -> +3.3V
- SW30 pad 2: Net-(U4-GPB2) -> /Button_RCD29/To_MCP_PIN
- SW31 pad 1: Net-(R33-Pad1) -> +3.3V
- SW31 pad 2: Net-(U4-GPB1) -> /Button_RCD30/To_MCP_PIN
- SW32 pad 1: Net-(R34-Pad1) -> +3.3V
- SW32 pad 2: Net-(U4-GPB0) -> /Button_RCD31/To_MCP_PIN
- SW4 pad 1: Net-(R6-Pad1) -> +3.3V
- SW4 pad 2: Net-(U3-GPA4) -> /Button_RCD3/To_MCP_PIN
- SW5 pad 1: Net-(R7-Pad1) -> +3.3V
- SW5 pad 2: Net-(U3-GPA3) -> /Button_RCD4/To_MCP_PIN
- SW6 pad 1: Net-(R8-Pad1) -> +3.3V
- SW6 pad 2: Net-(U3-GPA2) -> /Button_RCD5/To_MCP_PIN
- SW7 pad 1: Net-(R9-Pad1) -> +3.3V
- SW7 pad 2: Net-(U3-GPA1) -> /Button_RCD6/To_MCP_PIN
- SW8 pad 1: Net-(R10-Pad1) -> +3.3V
- SW8 pad 2: Net-(U3-GPA0) -> /Button_RCD7/To_MCP_PIN
- SW9 pad 1: Net-(R11-Pad1) -> +3.3V
- SW9 pad 2: Net-(U3-GPB7) -> /Button_RCD8/To_MCP_PIN
- U2 pad 17: Net-(U3-A0) -> Net-(R2-Pad2)
- U2 pad 18: Net-(U3-A0) -> Net-(R2-Pad2)
- U2 pad 19: Net-(U1-3V) -> Net-(U2-PB8)
- U2 pad 20: Net-(U1-3V) -> Net-(U2-PB9)
- U3 pad 1: Net-(U3-GPB0) -> /Button_RCD13/To_MCP_PIN
- U3 pad 10: unconnected-(U3-VSS-Pad10) -> GND
- U3 pad 12: Net-(U1-3V) -> Net-(U2-PB8)
- U3 pad 13: Net-(U1-3V) -> Net-(U2-PB9)
- U3 pad 15: Net-(U3-A0) -> GND
- U3 pad 16: Net-(U3-A0) -> GND
- U3 pad 17: Net-(U3-A0) -> GND
- U3 pad 18: unconnected-(U3-~{RESET}-Pad18) -> Net-(U3-~{RESET})
- U3 pad 2: Net-(U3-GPB1) -> /Button_RCD12/To_MCP_PIN
- U3 pad 21: Net-(U3-GPA0) -> /Button_RCD6/To_MCP_PIN
- U3 pad 22: Net-(U3-GPA1) -> /Button_RCD5/To_MCP_PIN
- U3 pad 23: Net-(U3-GPA2) -> /Button_RCD4/To_MCP_PIN
- U3 pad 24: Net-(U3-GPA3) -> /Button_RCD3/To_MCP_PIN
- U3 pad 25: Net-(U3-GPA4) -> /Button_RCD2/To_MCP_PIN
- U3 pad 26: Net-(U3-GPA5) -> /Button_RCD1/To_MCP_PIN
- U3 pad 27: Net-(U3-GPA6) -> /Button_RCD/To_MCP_PIN
- U3 pad 28: Net-(U3-GPA7) -> /Button_RCD14/To_MCP_PIN
- U3 pad 3: Net-(U3-GPB2) -> /Button_RCD11/To_MCP_PIN
- U3 pad 4: Net-(U3-GPB3) -> /Button_RCD10/To_MCP_PIN
- U3 pad 5: Net-(U3-GPB4) -> /Button_RCD9/To_MCP_PIN
- U3 pad 6: Net-(U3-GPB5) -> /Button_RCD8/To_MCP_PIN
- U3 pad 7: Net-(U3-GPB6) -> /Button_RCD15/To_MCP_PIN
- U3 pad 8: Net-(U3-GPB7) -> /Button_RCD7/To_MCP_PIN
- U3 pad 9: unconnected-(U3-VDD-Pad9) -> +3.3V
- U4 pad 1: Net-(U4-GPB0) -> /Button_RCD29/To_MCP_PIN
- U4 pad 10: unconnected-(U4-VSS-Pad10) -> GND
- U4 pad 12: Net-(U1-3V) -> Net-(U2-PB8)
- U4 pad 13: Net-(U1-3V) -> Net-(U2-PB9)
- U4 pad 15: Net-(U3-A0) -> GND
- U4 pad 16: Net-(U1-3V) -> GND
- U4 pad 17: Net-(U1-3V) -> +3.3V
- U4 pad 18: unconnected-(U4-~{RESET}-Pad18) -> Net-(U4-~{RESET})
- U4 pad 2: Net-(U4-GPB1) -> /Button_RCD28/To_MCP_PIN
- U4 pad 21: Net-(U4-GPA0) -> /Button_RCD22/To_MCP_PIN
- U4 pad 22: Net-(U4-GPA1) -> /Button_RCD21/To_MCP_PIN
- U4 pad 23: Net-(U4-GPA2) -> /Button_RCD20/To_MCP_PIN
- U4 pad 24: Net-(U4-GPA3) -> /Button_RCD19/To_MCP_PIN
- U4 pad 25: Net-(U4-GPA4) -> /Button_RCD18/To_MCP_PIN
- U4 pad 26: Net-(U4-GPA5) -> /Button_RCD17/To_MCP_PIN
- U4 pad 27: Net-(U4-GPA6) -> /Button_RCD16/To_MCP_PIN
- U4 pad 28: Net-(U4-GPA7) -> /Button_RCD30/To_MCP_PIN
- U4 pad 3: Net-(U4-GPB2) -> /Button_RCD27/To_MCP_PIN
- U4 pad 4: Net-(U4-GPB3) -> /Button_RCD26/To_MCP_PIN
- U4 pad 5: Net-(U4-GPB4) -> /Button_RCD25/To_MCP_PIN
- U4 pad 6: Net-(U4-GPB5) -> /Button_RCD24/To_MCP_PIN
- U4 pad 7: Net-(U4-GPB6) -> /Button_RCD31/To_MCP_PIN
- U4 pad 8: Net-(U4-GPB7) -> /Button_RCD23/To_MCP_PIN
- U4 pad 9: unconnected-(U4-VDD-Pad9) -> +3.3V

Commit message: ajout 2 mcp23017
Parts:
- C1, C10, C11, C12, C13, C14, C15, C16, C17, C18, C19, C2, C20, C21, C22, C23, C24, C25, C26, C27, C28, C29, C3, C30, C31, C32, C33, C4, C5, C6, C7, C8, C9: footprint Capacitor_THT:C_Disc_D3.0mm_W1.6mm_P2.50mm -> Capacitor_THT:CP_Axial_L10.0mm_D4.5mm_P15.00mm_Horizontal
- R10, R11, R12, R13, R14, R15, R16, R17, R18, R19, R20, R21, R22, R23, R24, R25, R26, R27, R28, R29, R3, R30, R31, R32, R33, R34, R35, R36, R37, R38, R39, R4, R40, R5, R6, R7, R8, R9: footprint Resistor_THT:R_Axial_DIN0207_L6.3mm_D2.5mm_P7.62mm_Horizontal -> Resistor_SMD:R_0603_1608Metric
